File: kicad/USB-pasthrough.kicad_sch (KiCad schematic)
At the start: 93 parts, among them J1 USB_Power, J10 MicroSD, J4 Power_Sel, J5 SPI Display, J6 SWD, J7 Cortex Debug, J8 USB_C, J9 USB_A, SW1 Boot0, SW2 Reset, U1 STM32F723VET6, U2 AMS1117, Y1 8 MHz

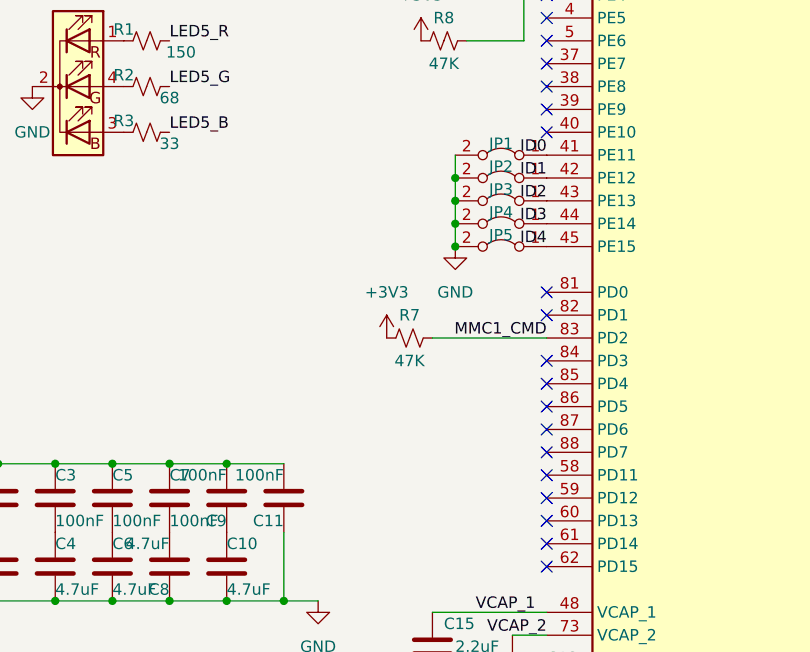
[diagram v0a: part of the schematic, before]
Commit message: Update schematic
Change JP2 to Open to reflect v0.2
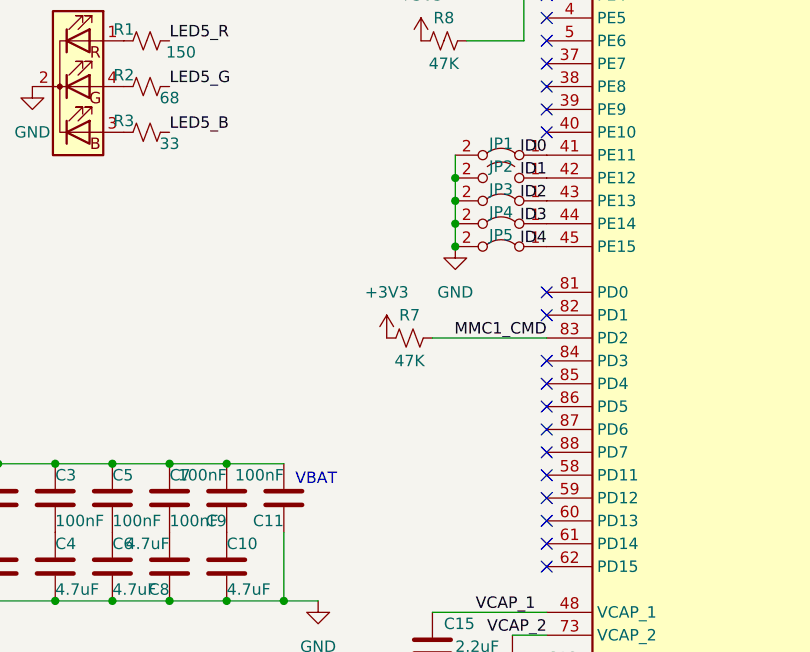
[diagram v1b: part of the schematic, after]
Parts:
- H1, H2, H3, H4: footprint MountingHole:MountingHole_3.2mm_M3_Pad -> MountingHole:MountingHole_2.2mm_M2_Pad
- JP2: footprint Jumper:SolderJumper-2_P1.3mm_Bridged_Pad1.0x1.5mm -> Jumper:SolderJumper-2_P1.3mm_Open_Pad1.0x1.5mm; symbol Jumper:Jumper_2_Bridged -> Jumper:Jumper_2_Open
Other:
- note added: "VBAT"
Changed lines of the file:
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@@
     (stroke (width 0) (type default) (color 0 0 0 0))
   )
+  (text "VBAT" (at 53.34 156.21 0)
+    (effects (font (size 1.27 1.27)) (justify left bottom))
+  )
   (label "SWCLK" (at 224.79 82.55 0)
     (effects (font (size 1.27 1.27)) (justify left bottom))
@@
     (pin "1")
   )
-  (symbol (lib_id "Jumper:Jumper_2_Bridged") (at 76.2 121.92 0) (mirror y) (unit 1)
+  (symbol (lib_id "Jumper:Jumper_2_Open") (at 76.2 121.92 0) (mirror y) (unit 1)
     (in_bom yes) (on_board yes)
     (property "Reference" "JP2" (id 0) (at 76.2 120.65 0))
@@
       (effects (font (size 1.27 1.27)) hide)
     )
-    (property "Footprint" "Jumper:SolderJumper-2_P1.3mm_Bridged_Pad1.0x1.5mm" (id 2) (at 76.2 121.92 0)
+    (property "Footprint" "Jumper:SolderJumper-2_P1.3mm_Open_Pad1.0x1.5mm" (id 2) (at 76.2 121.92 0)
       (effects (font (size 1.27 1.27)) hide)
     )
@@
   (symbol (lib_id "power:GND") (at 20.32 74.93 0) (unit 1)
     (in_bom yes) (on_board yes) (fields_autoplaced)
-    (property "Reference" "#PWR?" (id 0) (at 20.32 81.28 0)
+    (property "Reference" "#PWR0104" (id 0) (at 20.32 81.28 0)
       (effects (font (size 1.27 1.27)) hide)
     )
@@
   (symbol (lib_id "power:GND") (at 20.32 80.01 0) (unit 1)
     (in_bom yes) (on_board yes) (fields_autoplaced)
-    (property "Reference" "#PWR?" (id 0) (at 20.32 86.36 0)
+    (property "Reference" "#PWR0106" (id 0) (at 20.32 86.36 0)
       (effects (font (size 1.27 1.27)) hide)
     )
@@
   (symbol (lib_id "power:GND") (at 20.32 69.85 0) (unit 1)
     (in_bom yes) (on_board yes) (fields_autoplaced)
-    (property "Reference" "#PWR?" (id 0) (at 20.32 76.2 0)
+    (property "Reference" "#PWR0105" (id 0) (at 20.32 76.2 0)
       (effects (font (size 1.27 1.27)) hide)
     )
@@
   (symbol (lib_id "power:GND") (at 20.32 85.09 0) (unit 1)
     (in_bom yes) (on_board yes) (fields_autoplaced)
-    (property "Reference" "#PWR?" (id 0) (at 20.32 91.44 0)
+    (property "Reference" "#PWR0103" (id 0) (at 20.32 91.44 0)
       (effects (font (size 1.27 1.27)) hide)
     )
@@
       (effects (font (size 1.27 1.27)) (justify left))
     )
-    (property "Footprint" "MountingHole:MountingHole_3.2mm_M3_Pad" (id 2) (at 20.32 85.09 0)
+    (property "Footprint" "MountingHole:MountingHole_2.2mm_M2_Pad" (id 2) (at 20.32 85.09 0)
       (effects (font (size 1.27 1.27)) hide)
     )
@@
       (effects (font (size 1.27 1.27)) (justify left))
     )
-    (property "Footprint" "MountingHole:MountingHole_3.2mm_M3_Pad" (id 2) (at 20.32 80.01 0)
+    (property "Footprint" "MountingHole:MountingHole_2.2mm_M2_Pad" (id 2) (at 20.32 80.01 0)
       (effects (font (size 1.27 1.27)) hide)
     )
@@
       (effects (font (size 1.27 1.27)) (justify left))
     )
-    (property "Footprint" "MountingHole:MountingHole_3.2mm_M3_Pad" (id 2) (at 20.32 69.85 0)
+    (property "Footprint" "MountingHole:MountingHole_2.2mm_M2_Pad" (id 2) (at 20.32 69.85 0)
       (effects (font (size 1.27 1.27)) hide)
     )
@@
       (effects (font (size 1.27 1.27)) (justify left))
     )
-    (property "Footprint" "MountingHole:MountingHole_3.2mm_M3_Pad" (id 2) (at 20.32 74.93 0)
+    (property "Footprint" "MountingHole:MountingHole_2.2mm_M2_Pad" (id 2) (at 20.32 74.93 0)
       (effects (font (size 1.27 1.27)) hide)
     )
@@
       (reference "#PWR0102") (unit 1) (value "GND") (footprint "")
     )
-    (path "/2780cd65-fd11-479b-a112-83afcb948182"
-      (reference "#PWR?") (unit 1) (value "GND") (footprint "")
+    (path "/99afeda6-efb0-4d2e-b0cb-103121ecafc7"
+      (reference "#PWR0103") (unit 1) (value "GND") (footprint "")
     )
-    (path "/3e6c341a-fbb6-434a-9b04-9b417e443841"
-      (reference "#PWR?") (unit 1) (value "GND") (footprint "")
+    (path "/2780cd65-fd11-479b-a112-83afcb948182"
+      (reference "#PWR0104") (unit 1) (value "GND") (footprint "")
     )
     (path "/7b7cfd55-db82-4092-a1ab-1bd88b93d0b1"
-      (reference "#PWR?") (unit 1) (value "GND") (footprint "")
+      (reference "#PWR0105") (unit 1) (value "GND") (footprint "")
     )
-    (path "/99afeda6-efb0-4d2e-b0cb-103121ecafc7"
-      (reference "#PWR?") (unit 1) (value "GND") (footprint "")
+    (path "/3e6c341a-fbb6-434a-9b04-9b417e443841"
+      (reference "#PWR0106") (unit 1) (value "GND") (footprint "")
     )
     (path "/25f0af4b-4c86-454a-9084-b4f221f49eba"
@@
     )
     (path "/f160a860-25c2-4f66-9760-43f13b47f86b"
-      (reference "H1") (unit 1) (value "MountingHole") (footprint "MountingHole:MountingHole_3.2mm_M3_Pad")
+      (reference "H1") (unit 1) (value "MountingHole") (footprint "MountingHole:MountingHole_2.2mm_M2_Pad")
     )
     (path "/f2e2fe8f-a643-460d-8eb5-aa06bb423e01"
-      (reference "H2") (unit 1) (value "MountingHole") (footprint "MountingHole:MountingHole_3.2mm_M3_Pad")
+      (reference "H2") (unit 1) (value "MountingHole") (footprint "MountingHole:MountingHole_2.2mm_M2_Pad")
     )
     (path "/accccdd8-12e2-4161-b10b-5bfef537426e"
-      (reference "H3") (unit 1) (value "MountingHole") (footprint "MountingHole:MountingHole_3.2mm_M3_Pad")
+      (reference "H3") (unit 1) (value "MountingHole") (footprint "MountingHole:MountingHole_2.2mm_M2_Pad")
     )
     (path "/a809c965-2d99-474c-aca6-b23689d2fa7a"
-      (reference "H4") (unit 1) (value "MountingHole") (footprint "MountingHole:MountingHole_3.2mm_M3_Pad")
+      (reference "H4") (unit 1) (value "MountingHole") (footprint "MountingHole:MountingHole_2.2mm_M2_Pad")
     )
     (path "/7cf7e8fc-d4c5-4161-b905-d74139026239"
@@
     )
     (path "/1586b523-a3cf-43e8-bf9d-0533c598fcc1"
-      (reference "JP2") (unit 1) (value "Jumper_2_Bridged") (footprint "Jumper:SolderJumper-2_P1.3mm_Bridged_Pad1.0x1.5mm")
+      (reference "JP2") (unit 1) (value "Jumper_2_Bridged") (footprint "Jumper:SolderJumper-2_P1.3mm_Open_Pad1.0x1.5mm")
     )
     (path "/8d554622-7ff9-41d4-a107-16b60e1fce82"

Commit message: Update LED 2 footprint
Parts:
- LED2: footprint Resistor_SMD:R_0603_1608Metric_Pad0.98x0.95mm_HandSolder -> LED_SMD:LED_0603_1608Metric_Pad1.05x0.95mm_HandSolder
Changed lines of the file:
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@@
     (property "Reference" "LED2" (id 0) (at 200.66 25.4 0))
     (property "Value" "BLUE" (id 1) (at 201.93 17.78 0))
-    (property "Footprint" "Resistor_SMD:R_0603_1608Metric_Pad0.98x0.95mm_HandSolder" (id 2) (at 200.66 22.86 0)
+    (property "Footprint" "LED_SMD:LED_0603_1608Metric_Pad1.05x0.95mm_HandSolder" (id 2) (at 200.66 22.86 0)
       (effects (font (size 1.27 1.27)) hide)
     )
@@
     )
     (path "/853cd0b6-3a7d-4782-8733-3d029001cd41"
-      (reference "LED2") (unit 1) (value "BLUE") (footprint "Resistor_SMD:R_0603_1608Metric_Pad0.98x0.95mm_HandSolder")
+      (reference "LED2") (unit 1) (value "BLUE") (footprint "LED_SMD:LED_0603_1608Metric_Pad1.05x0.95mm_HandSolder")
     )
     (path "/0632b20a-c535-4fb7-8481-f3fee13a0c59"

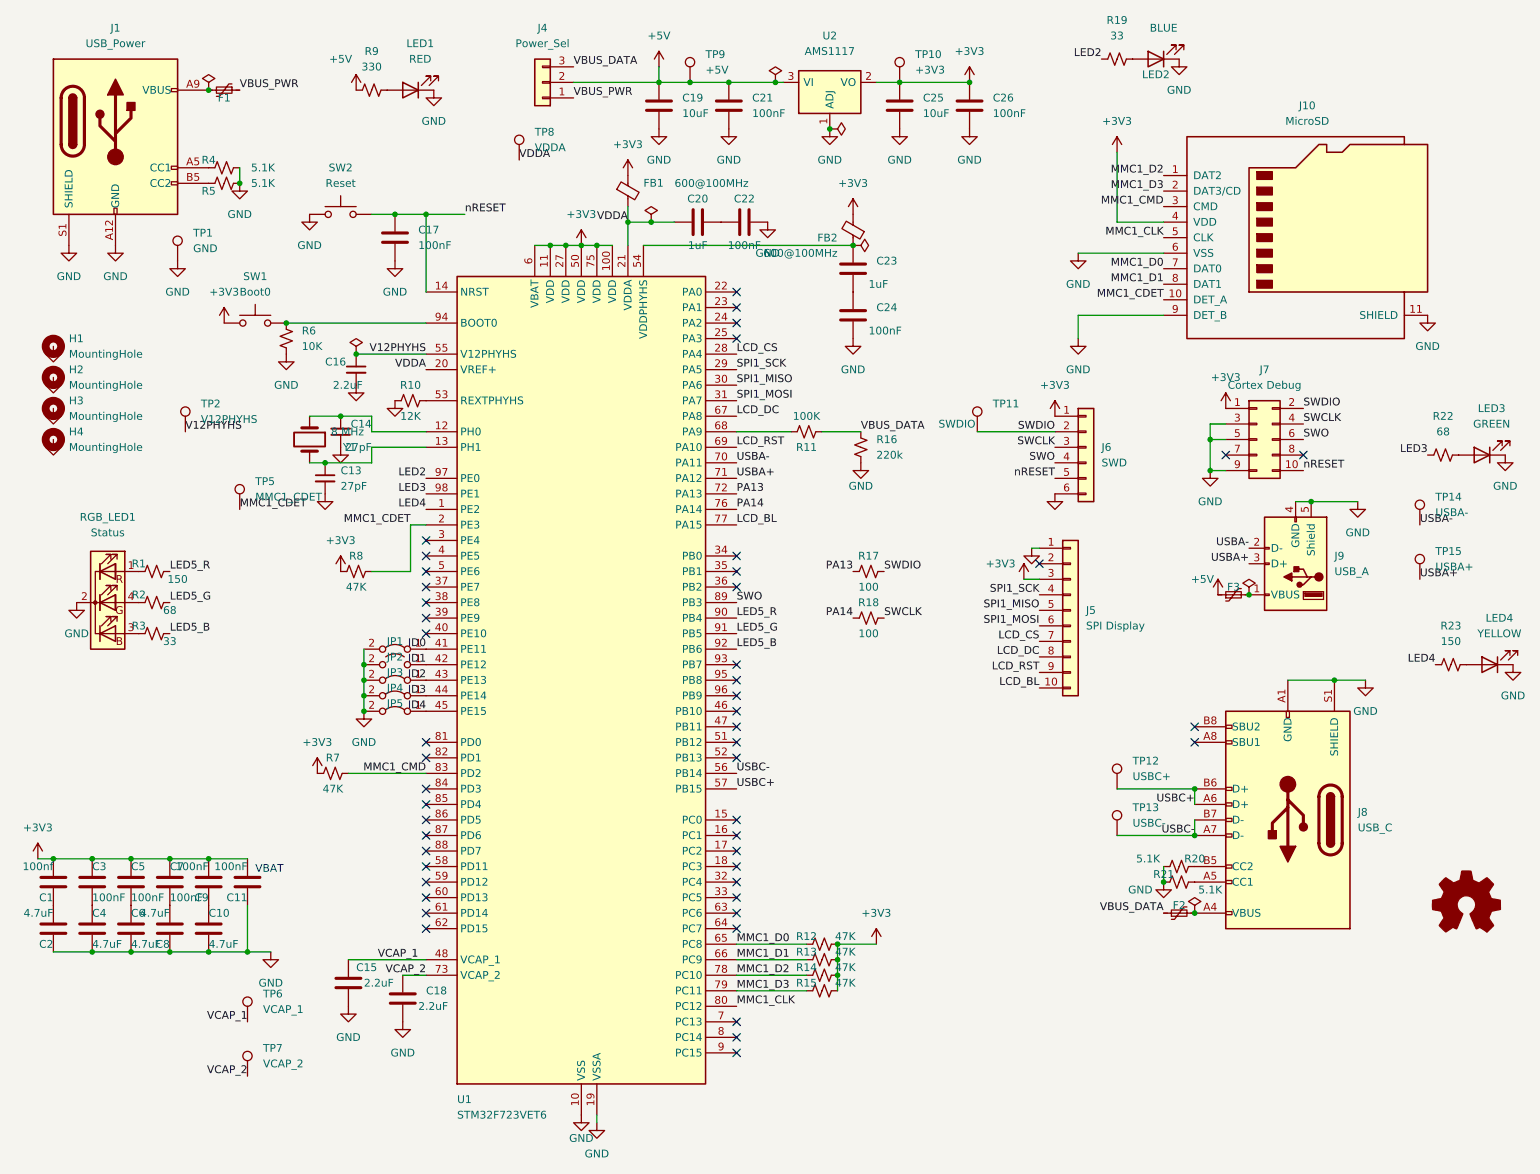
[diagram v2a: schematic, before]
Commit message: Realign pin 1 of components, up and left
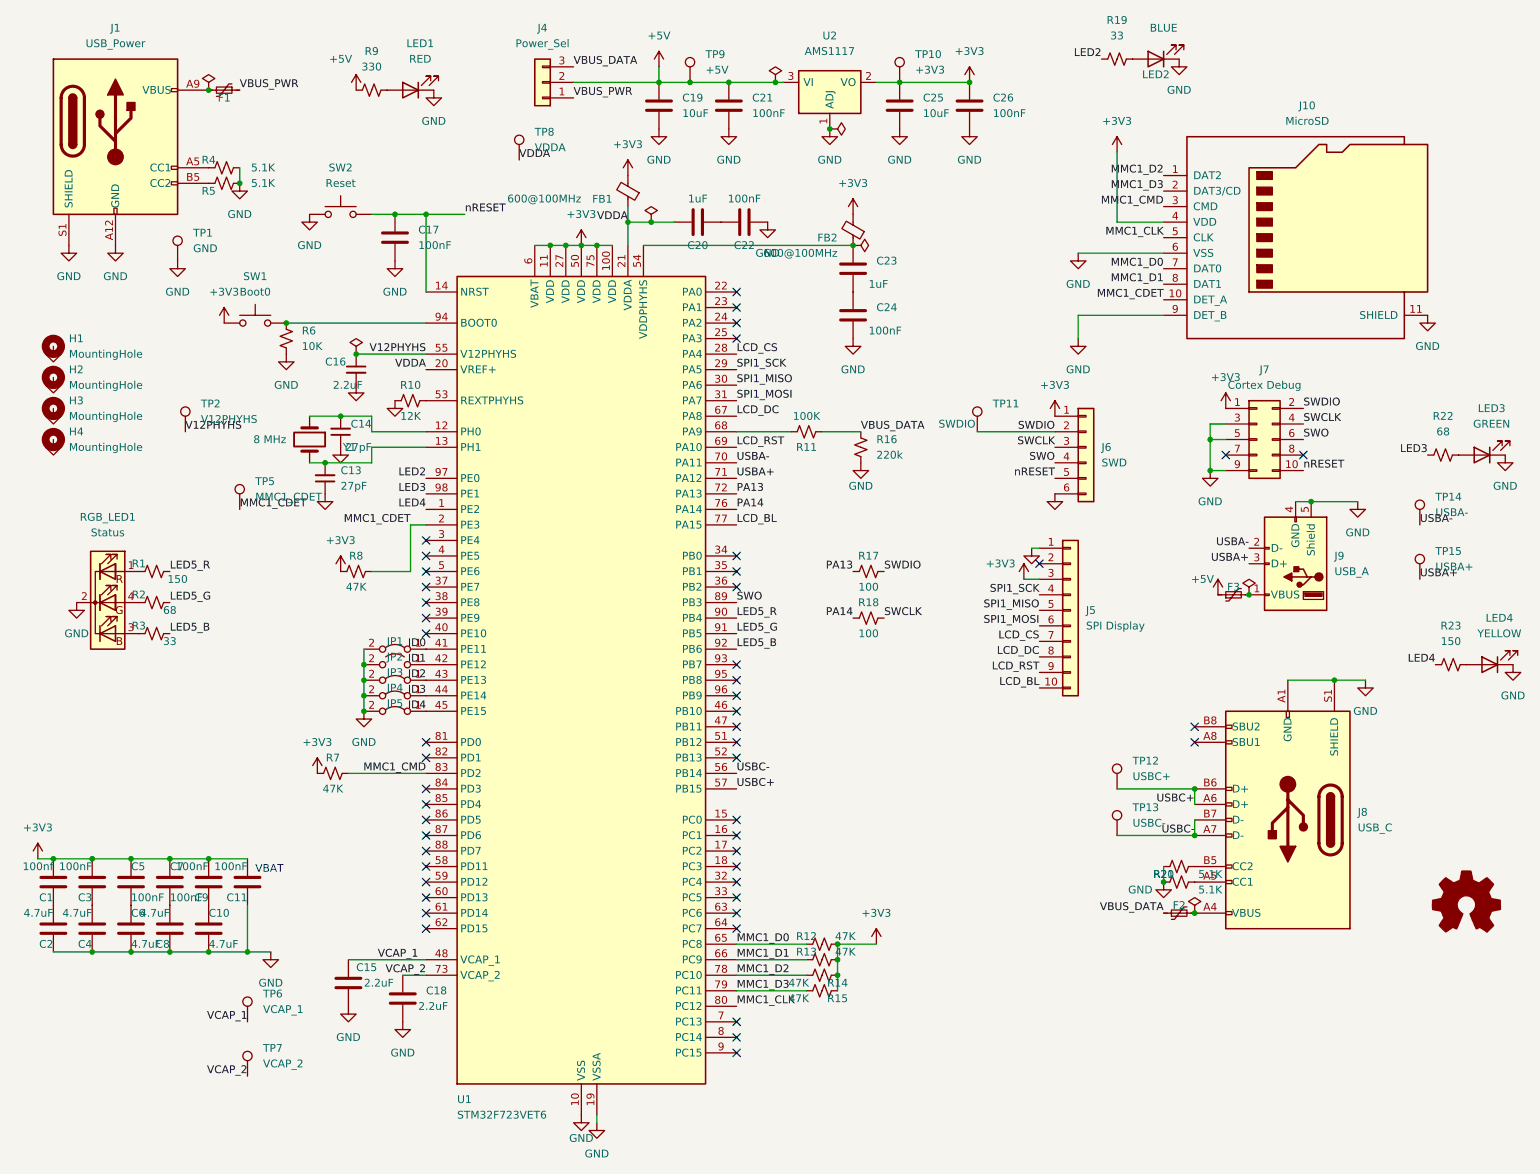
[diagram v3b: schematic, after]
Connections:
- net +3V3: now also C26.1, C3.2, FB1.2, R14.1, R15.1; no longer C26.2, C3.1, FB1.1, R14.2, R15.2
- net GND: now also C13.1, C22.2, C26.2, C4.1, R16.1, R20.2, R6.2; no longer C13.2, C22.1, C26.1, C4.2, R16.2, R20.1, R6.1
- net MMC1_D2: now also R14.2; no longer R14.1
- net MMC1_D3: now also R15.2; no longer R15.1
- net VBUS_DATA: now also R16.2; no longer R16.1
- net VDDA: now also C20.1, FB1.1; no longer C20.2, FB1.2
- net at SW1.1, U1.94 (BOOT0): now also R6.1; no longer R6.2
- net at U1.13 (PH1), Y1.2: now also C13.2; no longer C13.1
- net at J8.B5 (CC2): now also R20.1; no longer R20.2
- new net: C3.1, C4.2
- new net: C20.2, C22.1
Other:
- moved on the sheet: C13, C20, C22, C26, C3, C4, FB1, R14, R15, R16, R20, R6
